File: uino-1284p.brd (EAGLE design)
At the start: 68.6 x 53.3 mm, 59 parts, among them IC1 LD117AS50TR, IC2 ATMEGA1284AU, J1 Micro USB, J2 M03X2, J4 M03X2, J5 IO, U1 ATMEGA8U2AU, X1 16MHz, X2 16MHz

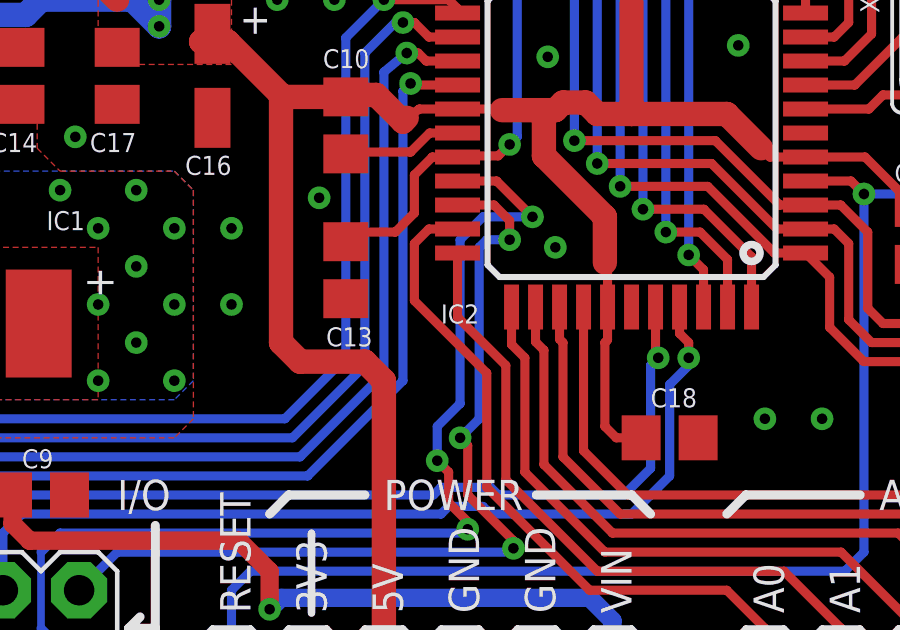
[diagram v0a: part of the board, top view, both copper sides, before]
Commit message: Made prefix for IC consistent.
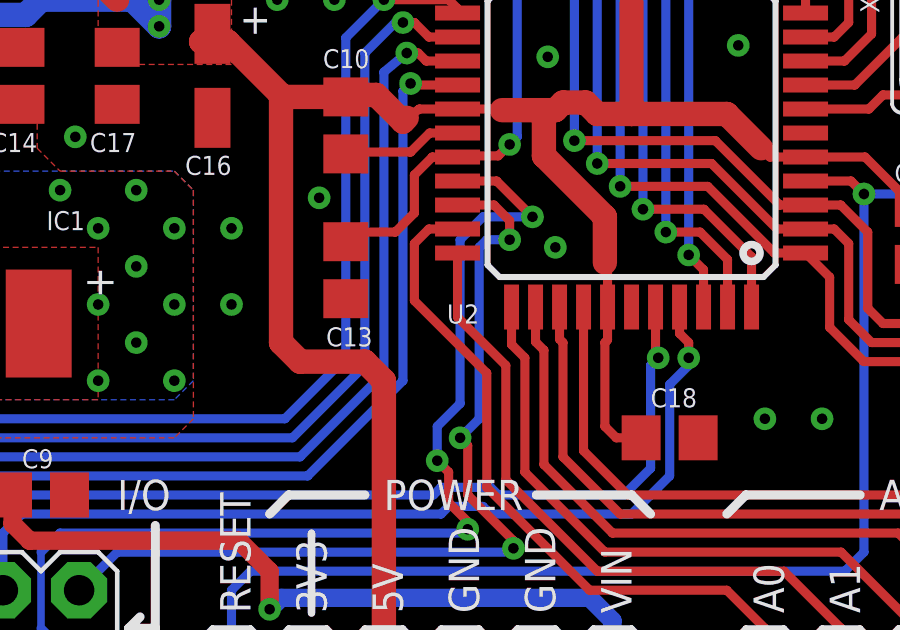
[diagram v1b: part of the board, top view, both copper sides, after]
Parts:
- removed IC2: ATMEGA1284AU, adilinden:TQFP44
- added U2: ATMEGA1284AU, adi-atmega:TQFP44
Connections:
- net A0: now also U2.32; no longer IC2.32
- net A1: now also U2.33; no longer IC2.33
- net A2: now also U2.34; no longer IC2.34
- net A3: now also U2.35; no longer IC2.35
- net A4: now also U2.36; no longer IC2.36
- net A5: now also U2.37; no longer IC2.37
- net A6: now also U2.30; no longer IC2.30
- net A7: now also U2.31; no longer IC2.31
- net AREF: now also U2.29; no longer IC2.29
- net D0: now also U2.9; no longer IC2.9
- net D1: now also U2.10; no longer IC2.10
- net D18: now also U2.23; no longer IC2.23
- net D19: now also U2.24; no longer IC2.24
- net D2: now also U2.11; no longer IC2.11
- net D20: now also U2.25; no longer IC2.25
- net D21: now also U2.26; no longer IC2.26
- net D22: now also U2.40; no longer IC2.40
- net D23: now also U2.41; no longer IC2.41
- net D3: now also U2.12; no longer IC2.12
- net D4: now also U2.13; no longer IC2.13
- net D5: now also U2.14; no longer IC2.14
- net D6: now also U2.15; no longer IC2.15
- net D7: now also U2.16; no longer IC2.16
- net D8: now also U2.42; no longer IC2.42
- net D9: now also U2.43; no longer IC2.43
- net GND: now also U2.18, U2.28, U2.39, U2.6; no longer IC2.18, IC2.28, IC2.39, IC2.6
- net L1: now also U2.21; no longer IC2.21
- net L2: now also U2.22; no longer IC2.22
- net MISO: now also U2.2; no longer IC2.2
- net MOSI: now also U2.1; no longer IC2.1
- net N$23: now also U2.8; no longer IC2.8
- net N$24: now also U2.7; no longer IC2.7
- net RESET: now also U2.4; no longer IC2.4
- net SCK: now also U2.3; no longer IC2.3
- net SCL: now also U2.19; no longer IC2.19
- net SDA: now also U2.20; no longer IC2.20
- net SS: now also U2.44; no longer IC2.44
- net VCC: now also U2.17, U2.27, U2.38, U2.5; no longer IC2.17, IC2.27, IC2.38, IC2.5

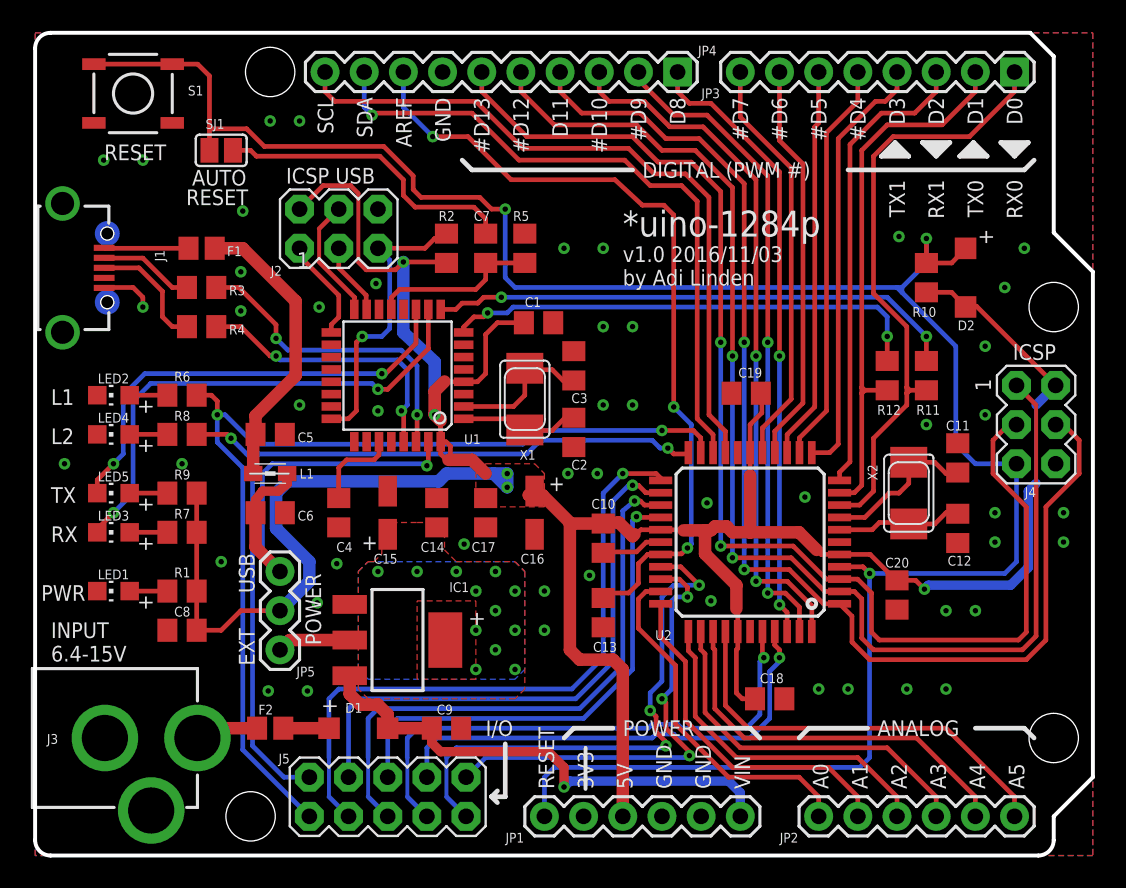
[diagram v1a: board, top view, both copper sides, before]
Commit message: Moved VCC lines. Fixed more naming.
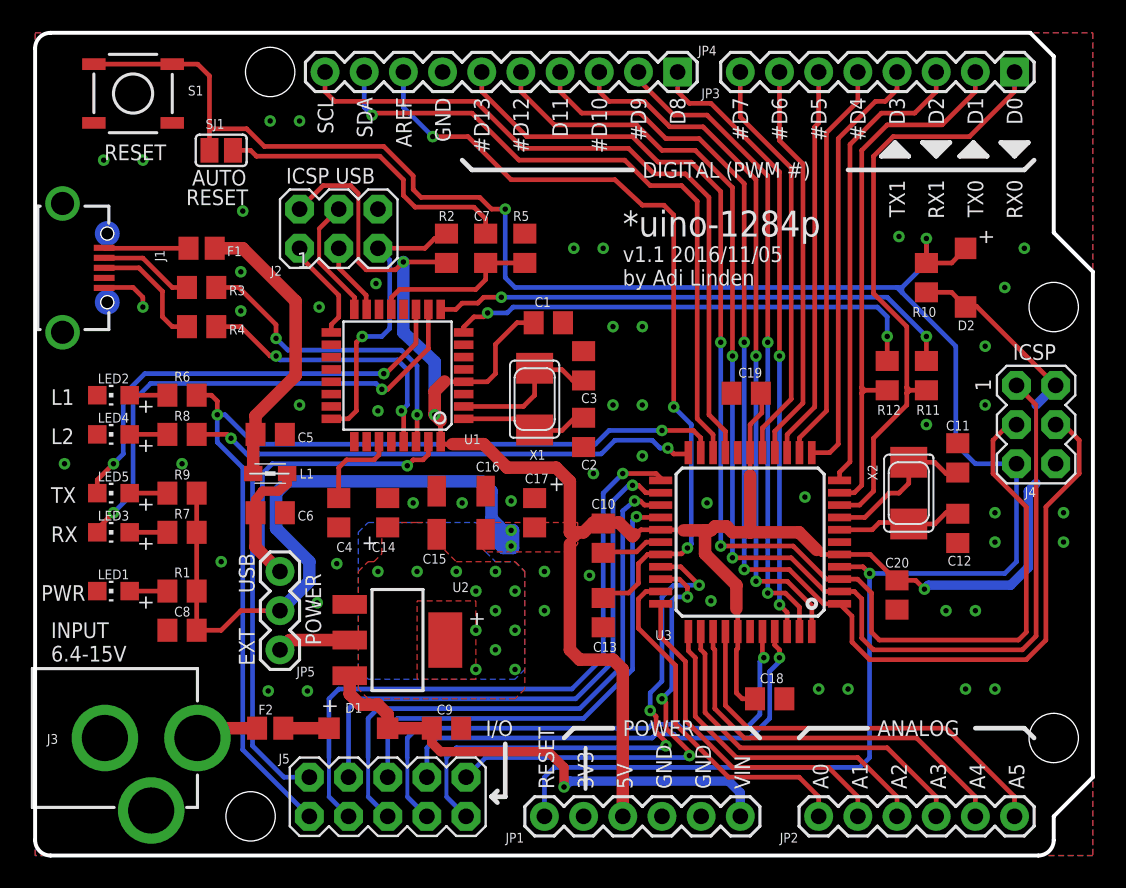
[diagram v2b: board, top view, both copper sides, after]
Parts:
- removed IC1: LD117AS50TR, adilinden:SOT223
- added U3: ATMEGA1284AU, adi-atmega:TQFP44
- F1: value 500mA -> 350mA
- F2: value 800mA -> 750mA
- U2: value ATMEGA1284AU -> LD117AS50TR; device adi-atmega:TQFP44 -> adi-misc:SOT223
- moved U2 23.7 mm to (23.5, 14.0), turned to 270 degrees
- moved C14 3.18 mm to (22.9, 22.2)
- moved C15 3.18 mm to (26.0, 22.2)
- moved C16 3.17 mm to (29.2, 22.2), turned to 90 degrees
- moved C17 3.17 mm to (32.4, 22.2), turned to 90 degrees
- moved C2 0.64 mm to (35.6, 27.4)
- moved C3 0.64 mm to (35.6, 31.8)
- moved C1 0.63 mm to (33.3, 34.5)
- moved X1 0.63 mm to (32.4, 29.6)
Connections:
- net A0: now also U3.32; no longer U2.32
- net A1: now also U3.33; no longer U2.33
- net A2: now also U3.34; no longer U2.34
- net A3: now also U3.35; no longer U2.35
- net A4: now also U3.36; no longer U2.36
- net A5: now also U3.37; no longer U2.37
- net A6: now also U3.30; no longer U2.30
- net A7: now also U3.31; no longer U2.31
- net AREF: now also U3.29; no longer U2.29
- net D0: now also U3.9; no longer U2.9
- net D1: now also U3.10; no longer U2.10
- net D18: now also U3.23; no longer U2.23
- net D19: now also U3.24; no longer U2.24
- net D2: now also U3.11; no longer U2.11
- net D20: now also U3.25; no longer U2.25
- net D21: now also U3.26; no longer U2.26
- net D22: now also U3.40; no longer U2.40
- net D23: now also U3.41; no longer U2.41
- net D3: now also U3.12; no longer U2.12
- net D4: now also U3.13; no longer U2.13
- net D5: now also U3.14; no longer U2.14
- net D6: now also U3.15; no longer U2.15
- net D7: now also U3.16; no longer U2.16
- net D8: now also U3.42; no longer U2.42
- net D9: now also U3.43; no longer U2.43
- net EVCC: now also U2.2, U2.4; no longer IC1.2, IC1.4
- net GND: now also U2.1, U3.18, U3.28, U3.39, U3.6; no longer IC1.1, U2.18, U2.28, U2.39, U2.6
- net L1: now also U3.21; no longer U2.21
- net L2: now also U3.22; no longer U2.22
- net MISO: now also U3.2; no longer U2.2
- net MOSI: now also U3.1; no longer U2.1
- net N$23: now also U3.8; no longer U2.8
- net N$24: now also U3.7; no longer U2.7
- net RESET: now also U3.4; no longer U2.4
- net SCK: now also U3.3; no longer U2.3
- net SCL: now also U3.19; no longer U2.19
- net SDA: now also U3.20; no longer U2.20
- net SS: now also U3.44; no longer U2.44
- net VCC: now also U3.17, U3.27, U3.38, U3.5; no longer U2.17, U2.27, U2.38, U2.5
- net VIN: now also U2.3; no longer IC1.3
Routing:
- net VCC: track 190.0 -> 196.7 mm
- net N$9: track 9.69 -> 12.0 mm
- net N$8: track 7.79 -> 9.50 mm
- net GND: vias 50 -> 52
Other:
- board text added: "v1.1 2016/11/05"
- board text removed: "v1.0 2016/11/03"

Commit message: Changed power input jack to screw terminal.
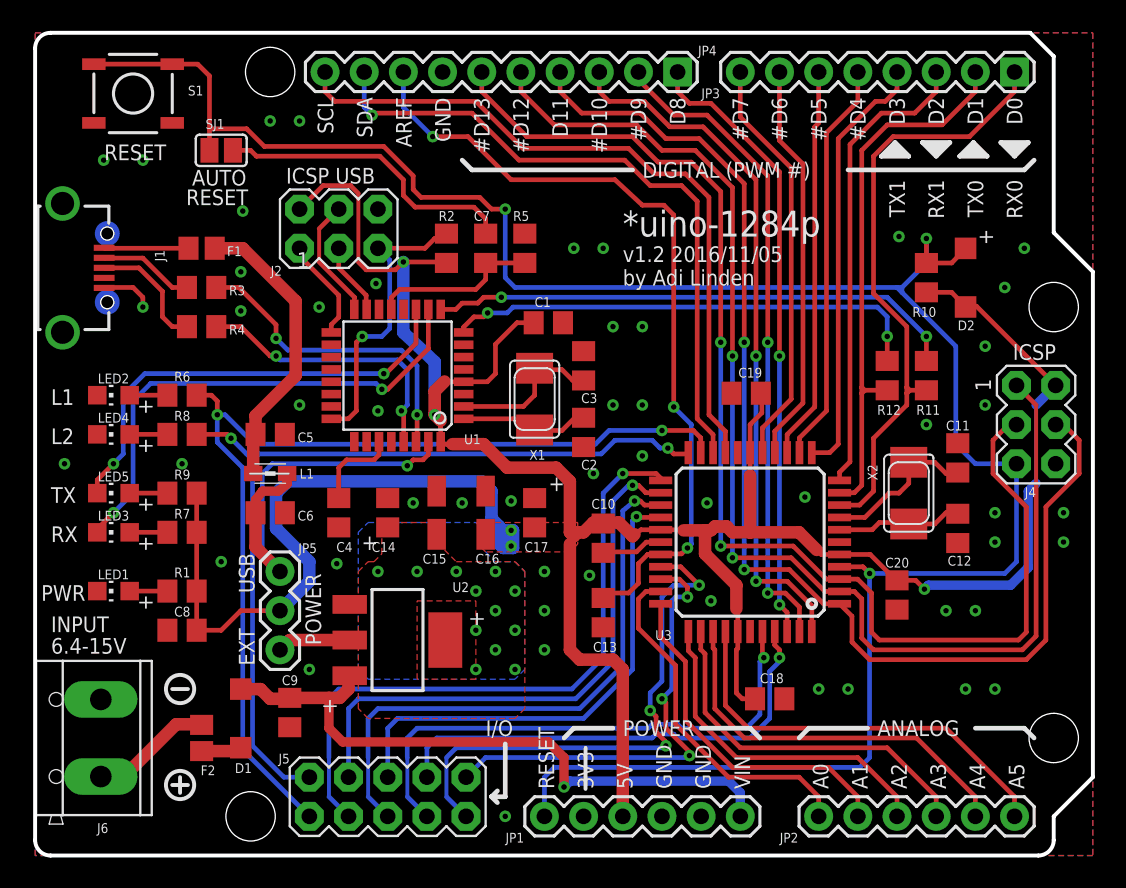
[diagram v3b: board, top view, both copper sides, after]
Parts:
- removed J3: (no value), SparkFun:POWER_JACK_PTH
- added J6: CON_TERMINAL_BLOCK_02-5MM, adi-misc:TERMINAL_BLOCK_2P_5
- moved C9 10.2 mm to (16.5, 9.27), turned to 270 degrees
- moved D1 7.65 mm to (13.3, 8.89), turned to 270 degrees
- moved F2 4.49 mm to (10.8, 7.62), turned to 270 degrees
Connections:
- removed net N$25: F2.1, J3.PWR
- new net N$17: F2.1, J6.2
- net GND: now also J6.1; no longer J3.GND, J3.GNDBREAK
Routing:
- net VIN: track 32.8 -> 41.7 mm
- net N$17: track 0.00 -> 7.95 mm
- net N$25: track 4.13 -> 0.00 mm
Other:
- board text added: "v1.2 2016/11/05"
- board text removed: "v1.1 2016/11/05"

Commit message: Renamed power jack.
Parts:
- renumbered J6 to J3
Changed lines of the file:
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@@
 <layer number="21" name="tPlace" color="7" fill="1" visible="yes" active="yes"/>
 <layer number="22" name="bPlace" color="7" fill="1" visible="yes" active="yes"/>
-<layer number="23" name="tOrigins" color="15" fill="1" visible="yes" active="yes"/>
-<layer number="24" name="bOrigins" color="15" fill="1" visible="yes" active="yes"/>
+<layer number="23" name="tOrigins" color="15" fill="1" visible="no" active="yes"/>
+<layer number="24" name="bOrigins" color="15" fill="1" visible="no" active="yes"/>
 <layer number="25" name="tNames" color="7" fill="1" visible="yes" active="yes"/>
 <layer number="26" name="bNames" color="7" fill="1" visible="no" active="yes"/>
@@
 <attribute name="VALUE" x="10.795" y="17.145" size="1.27" layer="27" rot="R180"/>
 </element>
-<element name="J6" library="adi-misc" package="TERMINAL_BLOCK_2P_5" value="CON_TERMINAL_BLOCK_02-5MM" x="3.81" y="7.62" smashed="yes" rot="R90">
+<element name="J3" library="adi-misc" package="TERMINAL_BLOCK_2P_5" value="CON_TERMINAL_BLOCK_02-5MM" x="3.81" y="7.62" smashed="yes" rot="R90">
 <attribute name="NAME" x="4.746" y="2.096" size="0.635" layer="25" rot="R180"/>
 </element>
@@
 <via x="24.511" y="22.86" extent="1-16" drill="0.35"/>
 <via x="30.861" y="22.987" extent="1-16" drill="0.35"/>
-<contactref element="J6" pad="1"/>
+<contactref element="J3" pad="1"/>
 </signal>
 <signal name="A0">
@@
 </signal>
 <signal name="N$17">
-<contactref element="J6" pad="2"/>
+<contactref element="J3" pad="2"/>
 <contactref element="F2" pad="1"/>
 <wire x1="4.26" y1="5.12" x2="5.755" y2="5.12" width="0.8128" layer="1"/>

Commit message: Changed power jack orientation.
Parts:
- moved J3 0.25 mm to (4.06, 7.62), turned to 270 degrees
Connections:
- net GND: now also J3.2; no longer J3.1
- net N$17: now also J3.1; no longer J3.2
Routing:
- net N$17: track 7.95 -> 8.57 mm
- net GND: vias 52 -> 54
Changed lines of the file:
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@@
 <attribute name="VALUE" x="10.795" y="17.145" size="1.27" layer="27" rot="R180"/>
 </element>
-<element name="J3" library="adi-misc" package="TERMINAL_BLOCK_2P_5" value="CON_TERMINAL_BLOCK_02-5MM" x="3.81" y="7.62" smashed="yes" rot="R90">
-<attribute name="NAME" x="4.746" y="2.096" size="0.635" layer="25" rot="R180"/>
+<element name="J3" library="adi-misc" package="TERMINAL_BLOCK_2P_5" value="CON_TERMINAL_BLOCK_02-5MM" x="4.064" y="7.62" smashed="yes" rot="R270">
+<attribute name="NAME" x="6.938" y="1.714" size="0.635" layer="25"/>
 </element>
 </elements>
@@
 <via x="24.511" y="22.86" extent="1-16" drill="0.35"/>
 <via x="30.861" y="22.987" extent="1-16" drill="0.35"/>
-<contactref element="J3" pad="1"/>
+<contactref element="J3" pad="2"/>
+<via x="3.81" y="1.905" extent="1-16" drill="0.35"/>
+<via x="10.795" y="3.175" extent="1-16" drill="0.35"/>
 </signal>
 <signal name="A0">
@@
 </signal>
 <signal name="N$17">
-<contactref element="J3" pad="2"/>
 <contactref element="F2" pad="1"/>
-<wire x1="4.26" y1="5.12" x2="5.755" y2="5.12" width="0.8128" layer="1"/>
-<wire x1="5.755" y1="5.12" x2="9.144" y2="8.509" width="0.8128" layer="1"/>
-<wire x1="9.144" y1="8.509" x2="10.756" y2="8.509" width="0.8128" layer="1"/>
-<wire x1="10.756" y1="8.509" x2="10.795" y2="8.47" width="0.8128" layer="1"/>
+<contactref element="J3" pad="1"/>
+<wire x1="3.614" y1="5.12" x2="5.755" y2="5.12" width="0.8128" layer="1"/>
+<wire x1="5.755" y1="5.12" x2="8.89" y2="8.255" width="0.8128" layer="1"/>
+<wire x1="8.89" y1="8.255" x2="10.58" y2="8.255" width="0.8128" layer="1"/>
+<wire x1="10.58" y1="8.255" x2="10.795" y2="8.47" width="0.8128" layer="1"/>
 </signal>
 </signals>

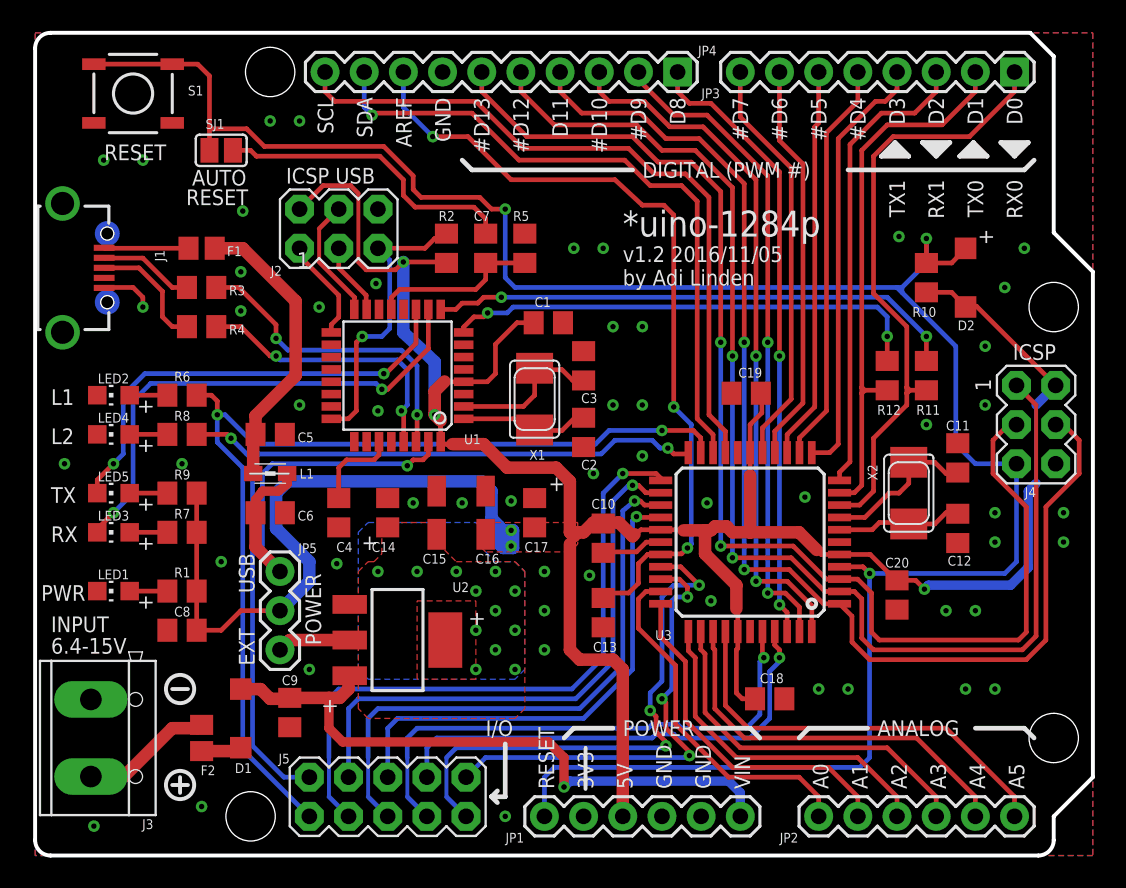
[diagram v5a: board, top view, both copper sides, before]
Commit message: Increased text sizes. Optimized polygon fills and routing.
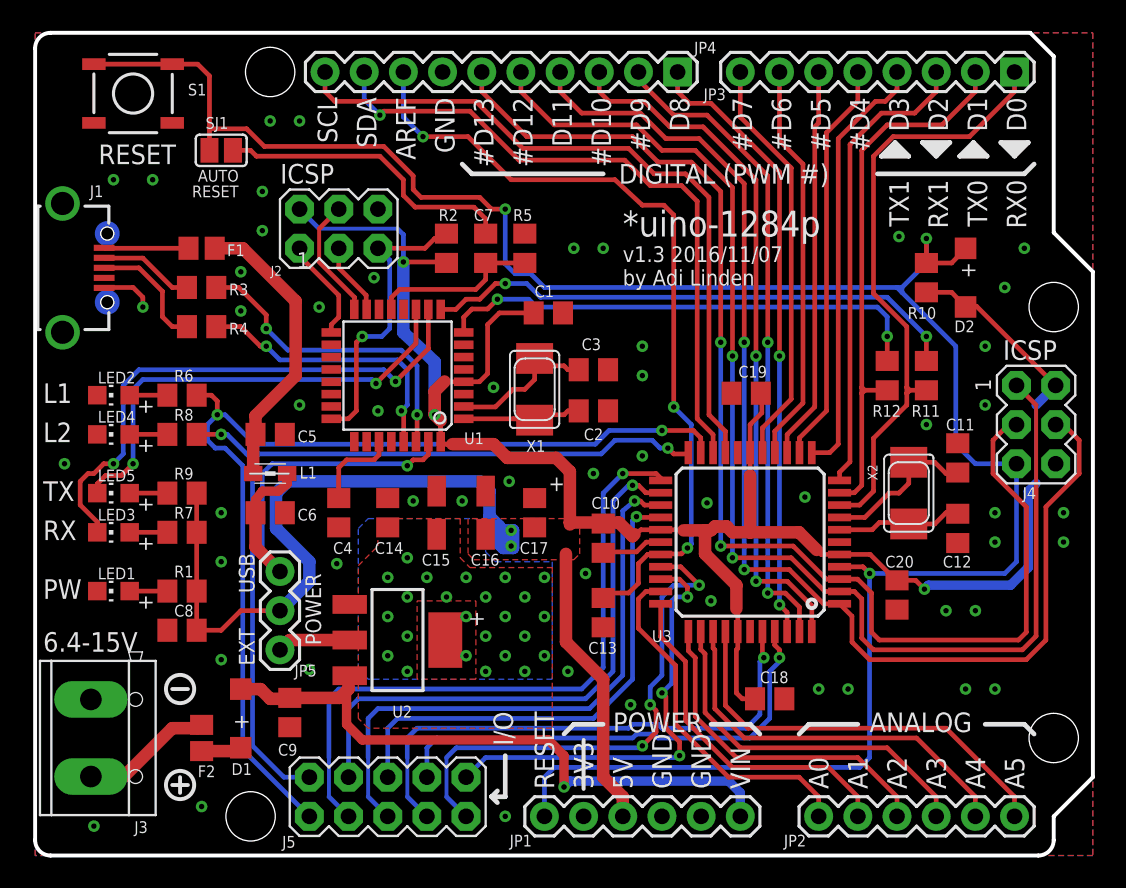
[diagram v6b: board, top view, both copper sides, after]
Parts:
- moved C2 1.53 mm to (36.2, 28.8), turned to 0 degrees
- moved C3 0.68 mm to (36.2, 31.5), turned to 0 degrees
- moved C1 0.64 mm to (33.3, 35.2)
- moved X1 0.63 mm to (32.4, 30.2)
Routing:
- net VCC: track 196.7 -> 192.0 mm
- net N$29: track 32.9 -> 35.7 mm
- net A6: track 35.0 -> 33.6 mm
- net N$9: track 12.0 -> 11.0 mm
- net A7: track 29.8 -> 28.9 mm
- net L1: track 64.5 -> 65.4 mm
- net N$8: track 9.50 -> 8.61 mm
- net N$7: track 31.5 -> 32.3 mm
- net VIN: track 41.7 -> 41.0 mm
- net N$6: track 34.5 -> 35.2 mm
- net N$30: track 29.6 -> 30.3 mm
- net RESET: track 144.2 -> 143.7 mm
- net EVCC: vias 12 -> 24
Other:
- board text added: "PW"
- board text added: "v1.3 2016/11/07"
- board text removed: "ICSP USB"
- board text removed: "INPUT"
- board text removed: "PWR"
- board text removed: "v1.2 2016/11/05"
